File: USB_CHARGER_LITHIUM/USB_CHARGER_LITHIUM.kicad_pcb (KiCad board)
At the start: 2 copper layers, 22 parts, among them J1 USB4135, J2 Conn_01x02, J3 Conn_01x02, U1 TP5000X-4.2-ESOP8, U2 XB7608A

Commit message: Placed components in pcb
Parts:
- removed H3: MountingHole, MountingHole:MountingHole_3.2mm_M3_DIN965_Pad
- moved H2 59.1 mm to (161.2, 69.2)
- moved C3 47.0 mm to (162.2, 62.2)
- moved C5 38.9 mm to (138.9, 56.5)
- moved U2 37.1 mm to (140.9, 52.1), turned to 90 degrees
- moved C4 36.7 mm to (146.6, 61.6)
- moved BAT 33.4 mm to (149.8, 52.8)
- moved R4 33.0 mm to (154.6, 62.2)
- moved U1 21.5 mm to (139.6, 65.4), turned to 90 degrees
- moved J1 21.2 mm to (114.8, 64.8), turned to -90 degrees
- moved R5 20.1 mm to (143.7, 56.5)
- moved D1 18.8 mm to (128.2, 72.7), turned to 90 degrees
- moved C2 18.6 mm to (133.2, 67.9), turned to 90 degrees
- moved Adafruit 17.6 mm to (159.9, 52.2)
- moved D2 17.5 mm to (132.0, 72.7), turned to 90 degrees
- moved H1 9.95 mm to (119.9, 52.7)
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- renumbered J3 to Adafruit, J2 to BAT
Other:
- board outline added: 55.9 x 29.2 mm

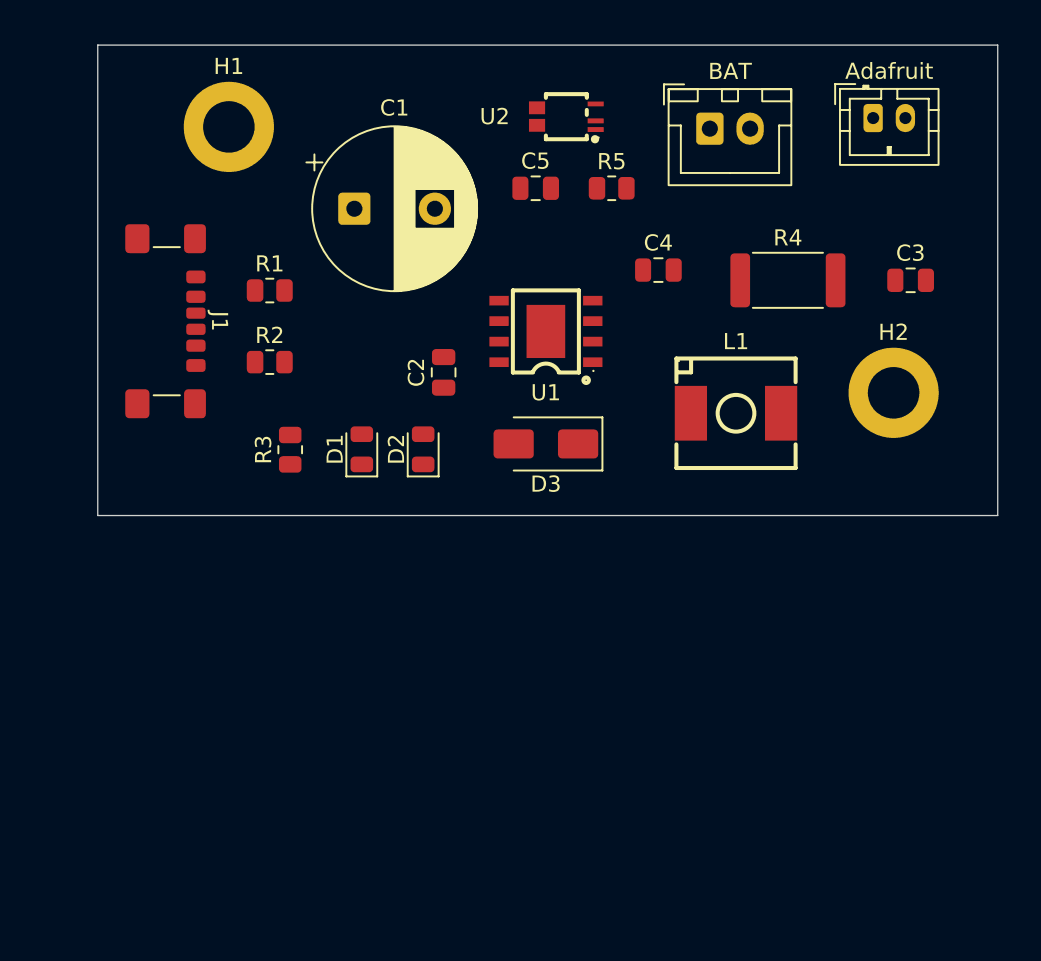
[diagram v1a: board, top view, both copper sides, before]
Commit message: Fixed shchematic grid and added ground copper planes
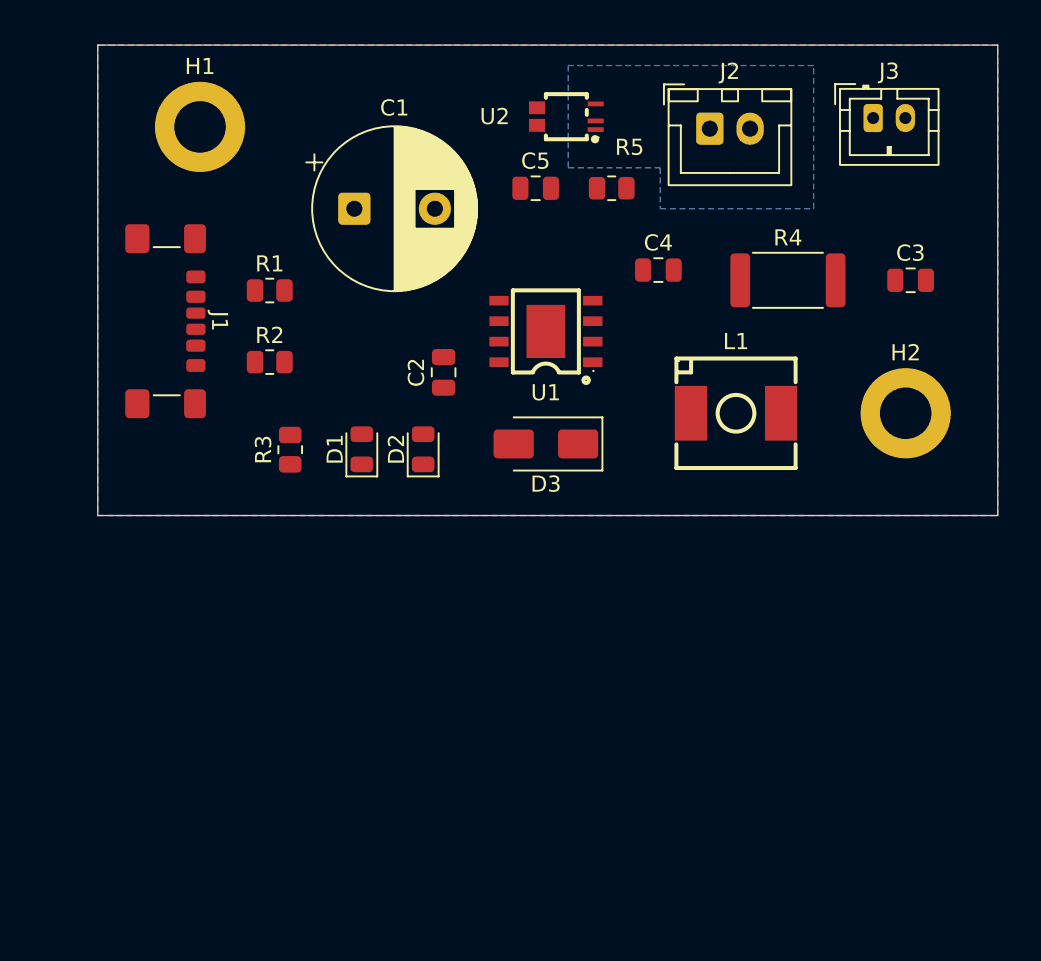
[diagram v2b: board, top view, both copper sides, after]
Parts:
- moved H1 1.79 mm to (118.1, 52.7)
- moved H2 1.47 mm to (161.9, 70.5)
- renumbered BAT to J2, Adafruit to J3
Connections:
- net Net-(J2-Pin_1) renamed +BATT
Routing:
- added copper zone on F.Cu, net (none)
- added copper zone on B.Cu, net GND
- added copper zone on B.Cu, net GNDPWR
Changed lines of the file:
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@@
 	(net 2 "GND")
 	(net 3 "Net-(U1-VS)")
-	(net 4 "Net-(J2-Pin_1)")
+	(net 4 "+BATT")
 	(net 5 "Net-(U2-VDD)")
 	(net 6 "Net-(D1-K)")
@@
 			(size 0.6 1.2)
 			(layers "F.Cu" "F.Mask" "F.Paste")
-			(net 4 "Net-(J2-Pin_1)")
+			(net 4 "+BATT")
 			(pinfunction "BAT")
 			(pintype "power_in")
@@
 			(layers "F.Cu" "F.Mask" "F.Paste")
 			(roundrect_rratio 0.25)
-			(net 4 "Net-(J2-Pin_1)")
+			(net 4 "+BATT")
 			(pintype "passive")
 		)
@@
 		(descr "JST PH series connector, B2B-PH-K (http://www.jst-mfg.com/product/pdf/eng/ePH.pdf), generated with kicad-footprint-generator")
 		(tags "connector JST PH vertical")
-		(property "Reference" "Adafruit"
+		(property "Reference" "J3"
 			(at 1 -2.9 0)
 			(layer "F.SilkS")
@@
 			(remove_unused_layers no)
 			(roundrect_rratio 0.208333)
-			(net 4 "Net-(J2-Pin_1)")
+			(net 4 "+BATT")
 			(pinfunction "Pin_1")
 			(pintype "passive")
@@
 		(tags "resistor")
 		(property "Reference" "R5"
-			(at 0 -1.65 0)
+			(at 1.1075 -2.54 0)
 			(layer "F.SilkS")
 			(effects
@@
 			(layers "F.Cu" "F.Mask" "F.Paste")
 			(roundrect_rratio 0.243902)
-			(net 4 "Net-(J2-Pin_1)")
+			(net 4 "+BATT")
 			(pintype "passive")
 		)
@@
 	(footprint "MountingHole:MountingHole_3.2mm_M3_DIN965_Pad"
 		(layer "F.Cu")
-		(at 119.9 52.705)
+		(at 118.11 52.705)
 		(descr "Mounting Hole 3.2mm, M3, generated by kicad-footprint-generator mountinghole.py")
 		(tags "mountinghole M3 DIN965")
@@
 	(footprint "MountingHole:MountingHole_3.2mm_M3_DIN965_Pad"
 		(layer "F.Cu")
-		(at 161.175 69.215)
+		(at 161.925 70.485)
 		(descr "Mounting Hole 3.2mm, M3, generated by kicad-footprint-generator mountinghole.py")
 		(tags "mountinghole M3 DIN965")
@@
 		(descr "JST XH series connector, B2B-XH-A (http://www.jst-mfg.com/product/pdf/eng/eXH.pdf), generated with kicad-footprint-generator")
 		(tags "connector JST XH vertical")
-		(property "Reference" "BAT"
+		(property "Reference" "J2"
 			(at 1.25 -3.55 0)
 			(layer "F.SilkS")
@@
 			(remove_unused_layers no)
 			(roundrect_rratio 0.147059)
-			(net 4 "Net-(J2-Pin_1)")
+			(net 4 "+BATT")
 			(pinfunction "Pin_1")
 			(pintype "passive")
@@
 			(layers "F.Cu" "F.Mask" "F.Paste")
 			(roundrect_rratio 0.204082)
-			(net 4 "Net-(J2-Pin_1)")
+			(net 4 "+BATT")
 			(pintype "passive")
 		)
@@
 		)
 		(property "Value" "XB7608A"
-			(at 0 5.825 90)
+			(at 2.54 0.115 180)
 			(layer "F.Fab")
 			(effects
@@
 		(layer "Edge.Cuts")
 	)
+	(zone
+		(net 0)
+		(net_name "")
+		(layer "F.Cu")
+		(hatch edge 0.5)
+		(priority 2)
+		(connect_pads
+			(clearance 1)
+		)
+		(min_thickness 0.25)
+		(filled_areas_thickness no)
+		(fill
+			(thermal_gap 0.5)
+			(thermal_bridge_width 0.5)
+			(island_removal_mode 1)
+			(island_area_min 10)
+		)
+		(polygon
+			(pts
+				(xy 111.76 47.625) (xy 111.76 76.835) (xy 167.64 76.835) (xy 167.64 47.625)
+			)
+		)
+	)
+	(zone
+		(net 2)
+		(net_name "GND")
+		(layer "B.Cu")
+		(hatch edge 0.5)
+		(connect_pads
+			(clearance 1.5)
+		)
+		(min_thickness 0.25)
+		(filled_areas_thickness no)
+		(fill yes
+			(thermal_gap 0.5)
+			(thermal_bridge_width 0.5)
+			(smoothing fillet)
+			(radius 2)
+		)
+		(polygon
+			(pts
+				(xy 111.76 47.625) (xy 111.76 76.835) (xy 167.64 76.835) (xy 167.64 47.625)
+			)
+		)
+	)
+	(zone
+		(net 12)
+		(net_name "GNDPWR")
+		(layer "B.Cu")
+		(hatch edge 0.5)
+		(priority 1)
+		(connect_pads
+			(clearance 1)
+		)
+		(min_thickness 0.25)
+		(filled_areas_thickness no)
+		(fill yes
+			(thermal_gap 0.5)
+			(thermal_bridge_width 0.5)
+			(smoothing fillet)
+			(radius 2)
+		)
+		(polygon
+			(pts
+				(xy 140.97 48.895) (xy 140.97 55.245) (xy 146.685 55.245) (xy 146.685 57.785) (xy 156.21 57.785)
+				(xy 156.21 48.895)
+			)
+		)
+	)
 	(embedded_fonts no)

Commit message: Finished pcb design. Working on BOM and Positions
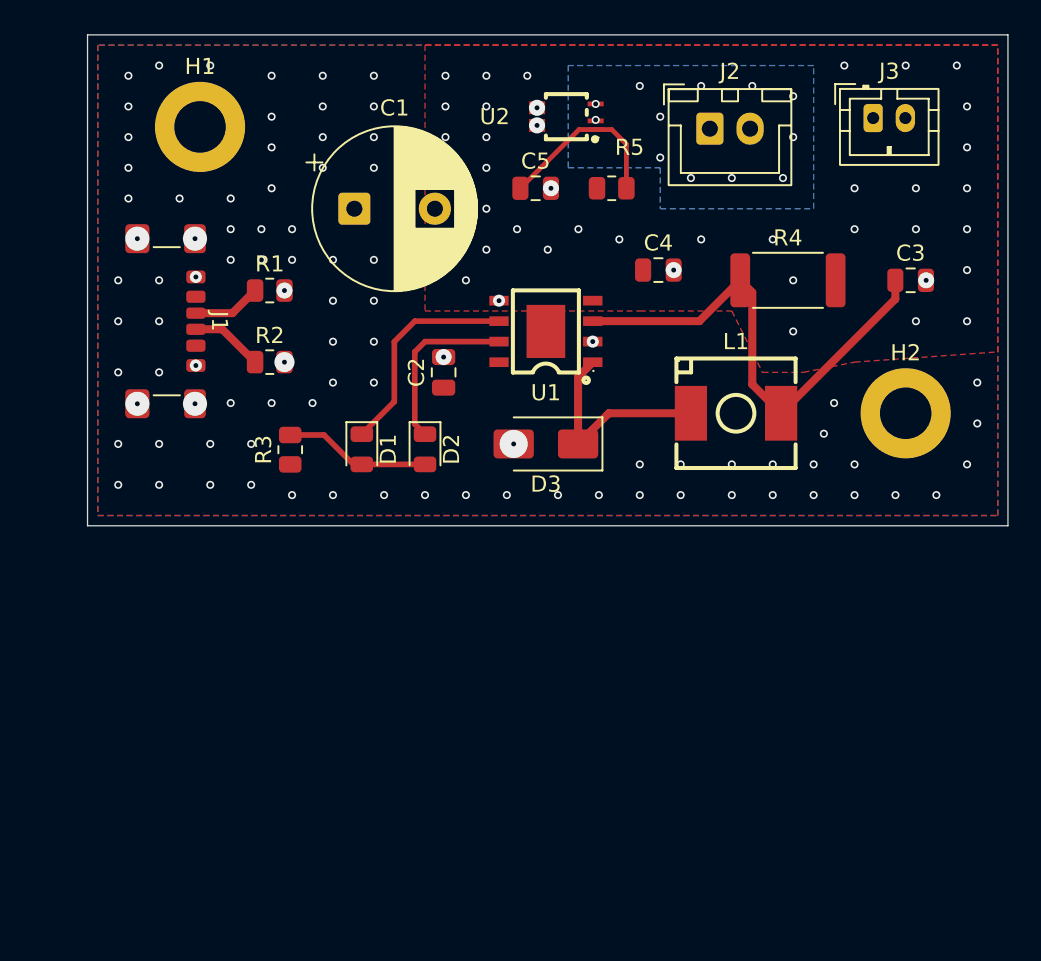
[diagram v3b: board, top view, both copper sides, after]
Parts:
- moved D2 0.12 mm to (132.1, 72.7), turned to -90 degrees
- turned D1 to -90 degrees
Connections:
- net Net-(U1-VIN) renamed VBUS
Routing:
- net Net-(U1-VS): track 0.00 -> 30.7 mm
- net Net-(D1-K): track 0.00 -> 13.6 mm
- net Net-(D3-K): track 0.00 -> 13.2 mm
- net Net-(U2-VDD): track 0.00 -> 11.2 mm
- net Net-(D2-K): track 0.00 -> 10.9 mm
- net Net-(D1-A): track 0.00 -> 9.13 mm
- net Net-(J1-CC2): track 0.00 -> 4.52 mm
- net Net-(J1-CC1): track 0.00 -> 4.26 mm
- net GNDPWR: track 0.00 -> 0.06 mm, vias 0 -> 12
- net GND: track 0.00 -> 0.01 mm, vias 0 -> 131
- added copper zone on F.Cu, net +BATT
- added copper zone on F.Cu, net VBUS
- removed copper zone on F.Cu, net (none)
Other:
- board size 55.9 x 29.2 mm -> 57.2 x 30.5 mm
- board text added: "ALMARAZ"
- board text added: "REV 1.0"
- board text added: "ROSALES"
- board text added: "VICTOR"

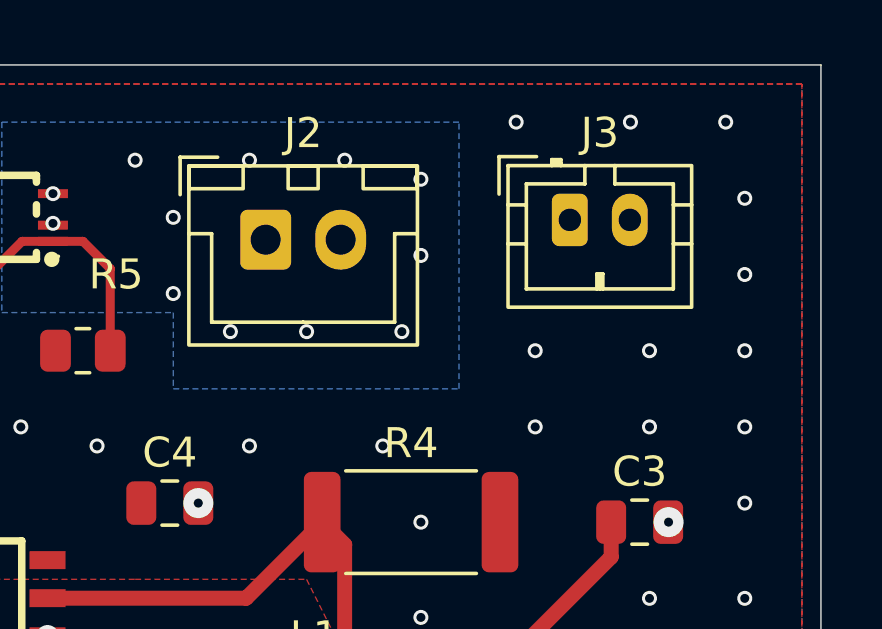
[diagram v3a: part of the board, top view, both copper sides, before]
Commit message: Gerber files, BOM, and positions files added
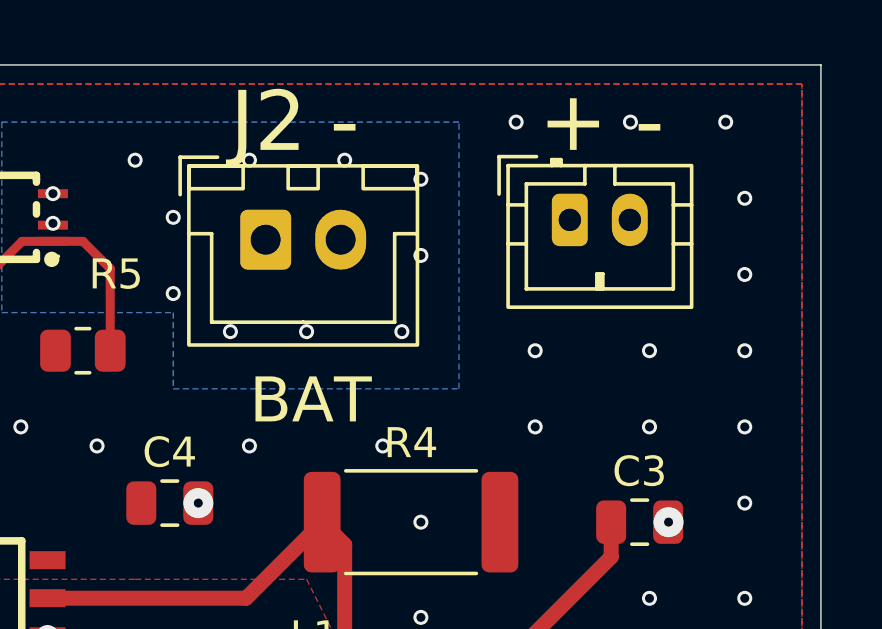
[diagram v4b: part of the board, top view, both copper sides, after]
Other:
- board text added: "+"
- board text added: "-"
- board text added: "BAT"
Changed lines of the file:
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@@
 			(outputformat 1)
 			(mirror no)
-			(drillshape 1)
+			(drillshape 0)
 			(scaleselection 1)
-			(outputdirectory "")
+			(outputdirectory "C:/Users/Victor Rosales/Documents/USB_Charger_2A/USB_CHARGER_LITHIUM/GerberFiles/DrillFiles/")
 		)
 	)
@@
 			(at 1 -2.9 0)
 			(layer "F.SilkS")
+			(hide yes)
 			(effects
 				(font
@@
 		(tags "connector JST XH vertical")
 		(property "Reference" "J2"
-			(at 1.25 -3.55 0)
+			(at 0.095 -3.92 0)
 			(layer "F.SilkS")
 			(effects
 				(font
-					(size 1 1)
-					(thickness 0.15)
+					(size 2 2)
+					(thickness 0.25)
 				)
 			)
@@
 		(layer "Edge.Cuts")
 	)
+	(gr_text "+"
+		(at 160.02 48.895 0)
+		(layer "F.SilkS")
+		(effects
+			(font
+				(size 2 2)
+				(thickness 0.25)
+			)
+		)
+	)
+	(gr_text "-"
+		(at 162.56 48.895 0)
+		(layer "F.SilkS")
+		(effects
+			(font
+				(size 2 2)
+				(thickness 0.25)
+			)
+		)
+	)
+	(gr_text "BAT"
+		(at 149.225 59.055 0)
+		(layer "F.SilkS")
+		(effects
+			(font
+				(size 1.5 1.5)
+				(thickness 0.25)
+			)
+			(justify left bottom)
+		)
+	)
+	(gr_text "-"
+		(at 152.4 48.895 0)
+		(layer "F.SilkS")
+		(effects
+			(font
+				(size 2 2)
+				(thickness 0.25)
+			)
+		)
+	)
 	(gr_text "ROSALES"

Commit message: Increased vias radius, and smoothed out corners
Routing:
- net GND: vias 131 -> 143
- net (no net): vias 0 -> 5
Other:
- outline, holes or cut-outs redrawn
